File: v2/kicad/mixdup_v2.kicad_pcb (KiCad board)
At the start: 2 copper layers, 96.5 x 189.2 mm, 38 parts, among them IC1 Teensy3.2, IC2 74HC4051, IC3 74HC4051, IC4 74HC4051, IC5 74HC4051, J1 Conn_02x10_Counter_Clockwise, SW1 SW_SPST, SW10 SW_SPST, SW11 SW_SPST, SW12 SW_SPST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

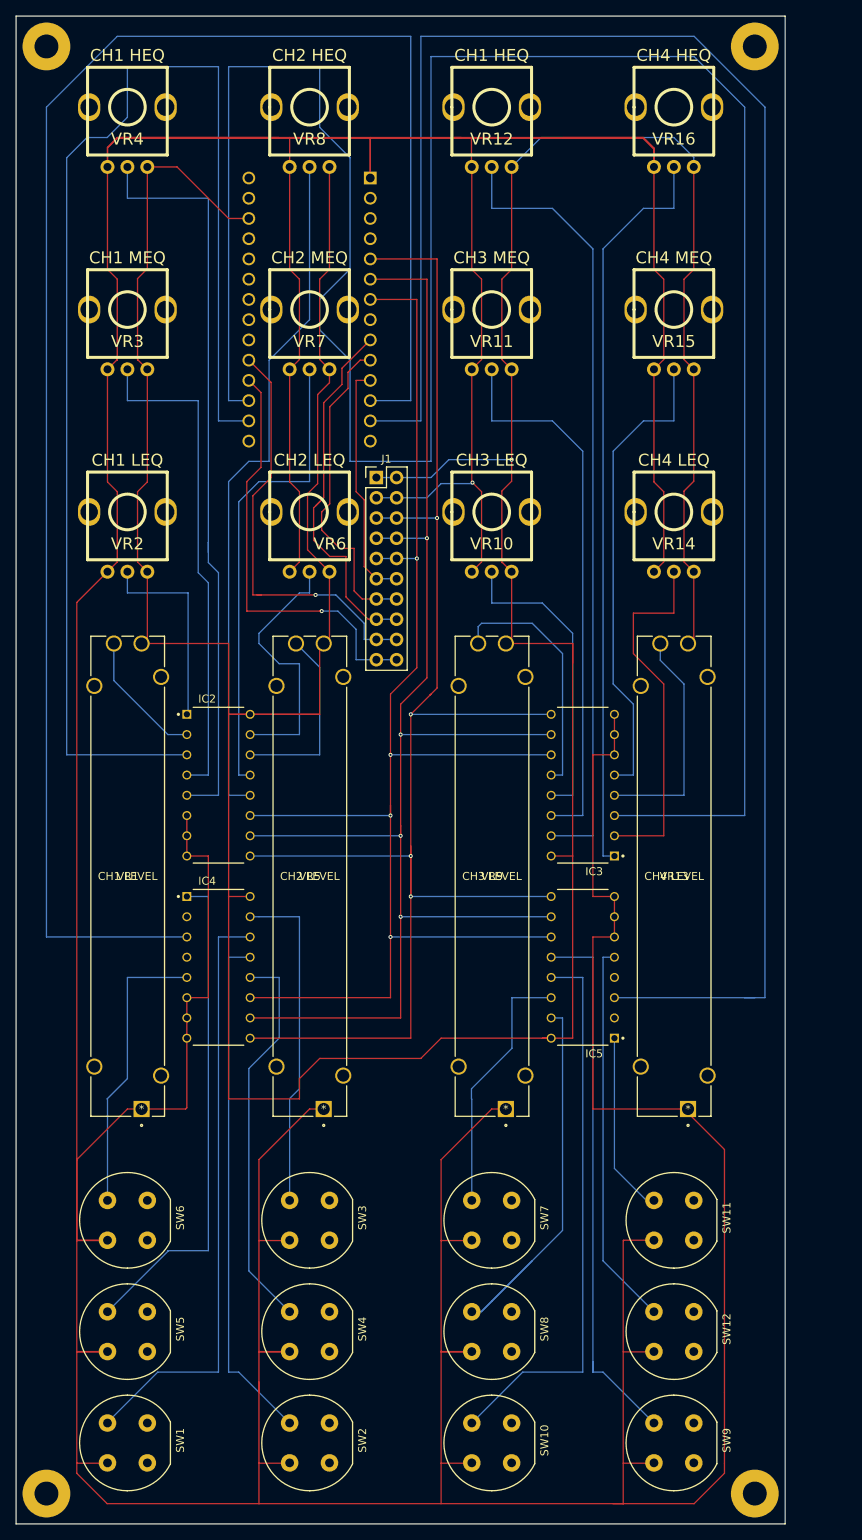
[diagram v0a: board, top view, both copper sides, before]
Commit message: components spaced out
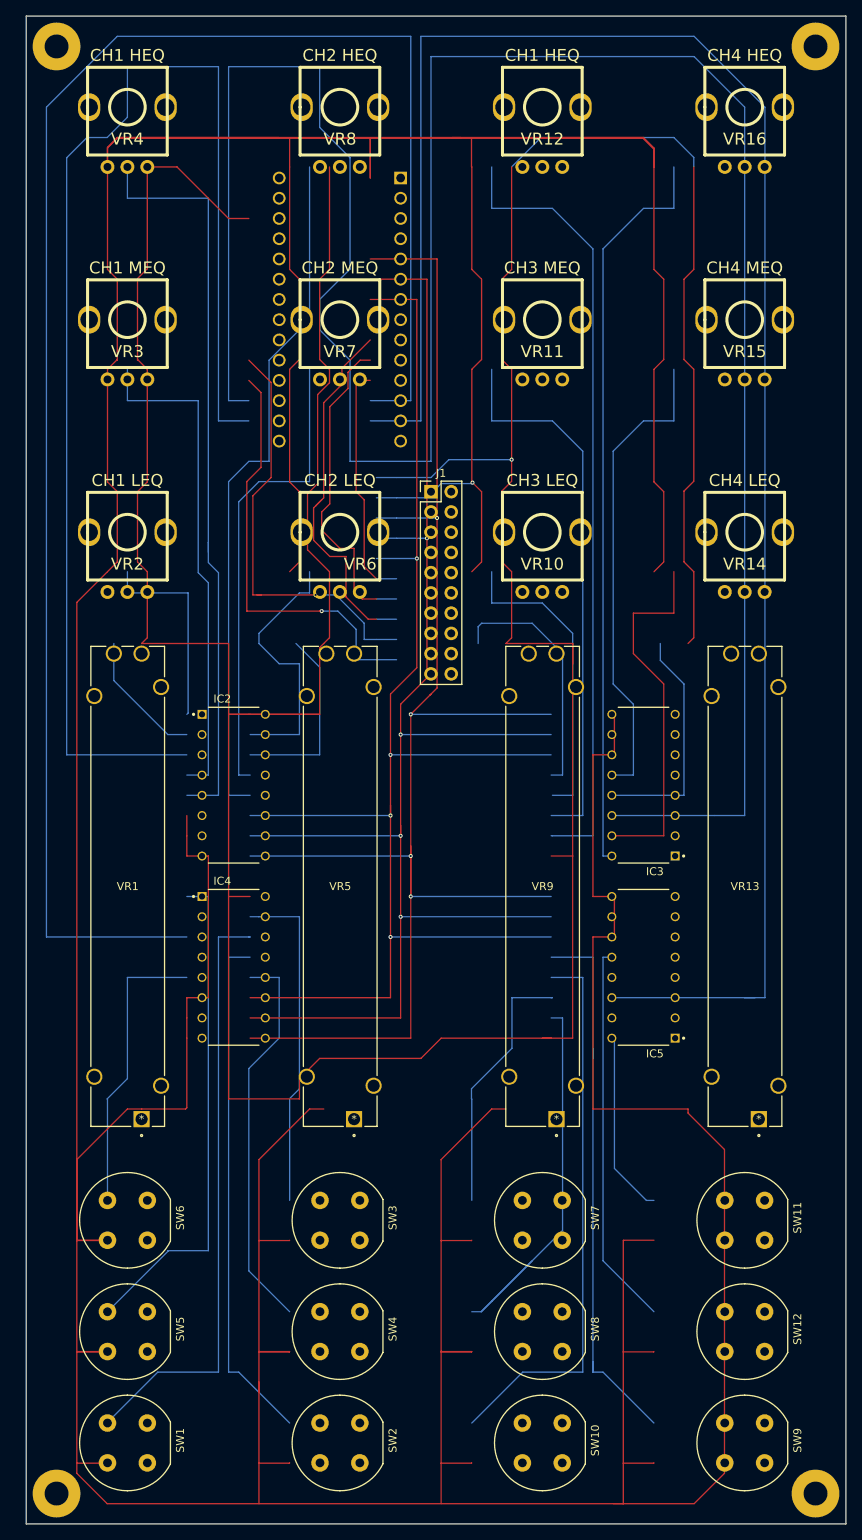
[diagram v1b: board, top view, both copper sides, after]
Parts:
- removed the ? at (222.2, 1139.2)
- removed the ? at (133.3, 1139.2)
- added ?: , MountingHole:MountingHole_3mm_Pad, F.Cu at (229.9, 1139.2)
- added ?: , MountingHole:MountingHole_3mm_Pad, F.Cu at (134.6, 1139.2)
- VR1: value CH1 LEVEL -> (none)
- VR13: value CH4 LEVEL -> (none)
- VR5: value CH2 LEVEL -> (none)
- VR9: value CH3 LEVEL -> (none)
- moved VR14 9.25 mm to (221.0, 1018.5)
- moved VR13 8.98 mm to (222.8, 1092.2)
- moved VR15 8.98 mm to (221.0, 991.9)
- moved SW11 8.89 mm to (221.0, 1104.9)
- moved SW12 8.89 mm to (221.0, 1118.9)
- moved SW9 8.89 mm to (221.0, 1132.8)
- moved VR16 8.89 mm to (221.0, 965.2)
- moved ? 7.62 mm to (229.9, 957.6)
- moved IC3 7.62 mm to (208.3, 1050.3)
- moved IC5 7.62 mm to (208.3, 1073.2)
- moved J1 7.08 mm to (181.6, 1013.5)
- moved VR10 6.84 mm to (195.6, 1018.5)
- moved VR11 6.48 mm to (195.6, 991.9)
- moved VR9 6.48 mm to (197.4, 1092.2)
- moved SW10 6.35 mm to (195.6, 1132.8)
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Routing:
- net VCC: track 524.7 -> 792.6 mm, vias 1 -> 2
- net (no net): track 0.00 -> 140.0 mm
- net Net-(IC3-Pad1): track 93.8 -> 0.00 mm
- net Net-(IC2-Pad12): track 87.3 -> 0.00 mm
- net Net-(IC3-Pad5): track 59.7 -> 0.00 mm
- net Net-(IC1-Pad23): track 54.1 -> 0.00 mm, vias 1 -> 0
- net Net-(IC5-Pad15): track 52.8 -> 0.00 mm
- net Net-(IC5-Pad12): track 70.2 -> 118.7 mm
- net Net-(IC5-Pad5): track 48.6 -> 0.00 mm
- net Net-(IC3-Pad15): track 98.9 -> 144.9 mm
- net Net-(IC3-Pad2): track 46.0 -> 0.00 mm
- net Net-(IC1-Pad9): track 46.7 -> 2.54 mm
- net Net-(IC2-Pad13): track 59.8 -> 103.9 mm
- net Net-(IC1-Pad10): track 40.7 -> 2.54 mm
- net Net-(IC3-Pad12): track 31.1 -> 59.7 mm
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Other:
- board size 96.5 x 189.2 mm -> 102.9 x 189.2 mm

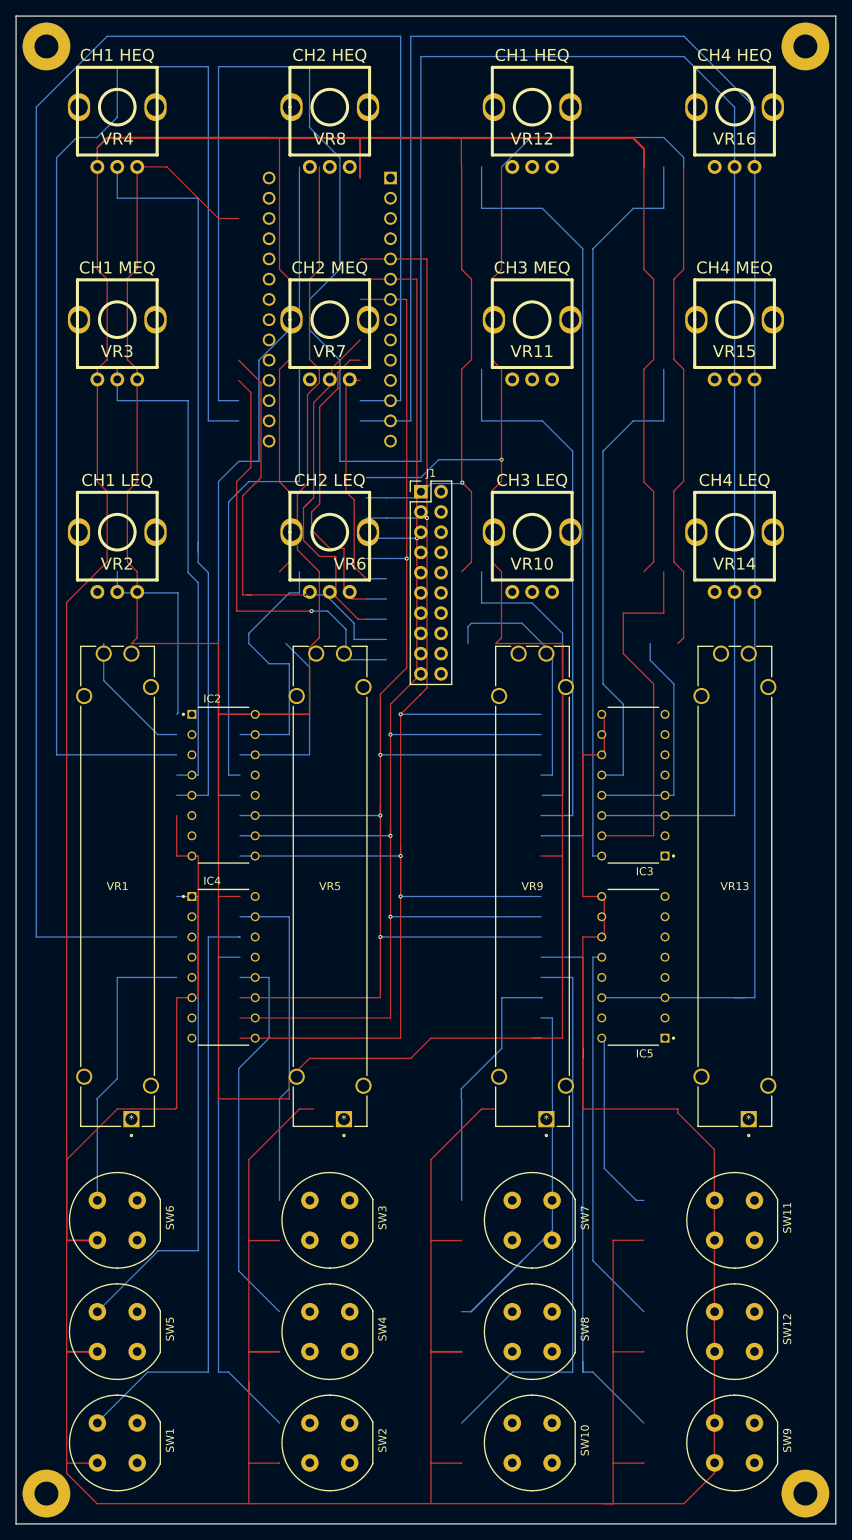
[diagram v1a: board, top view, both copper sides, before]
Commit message: better spacing, ICs on back
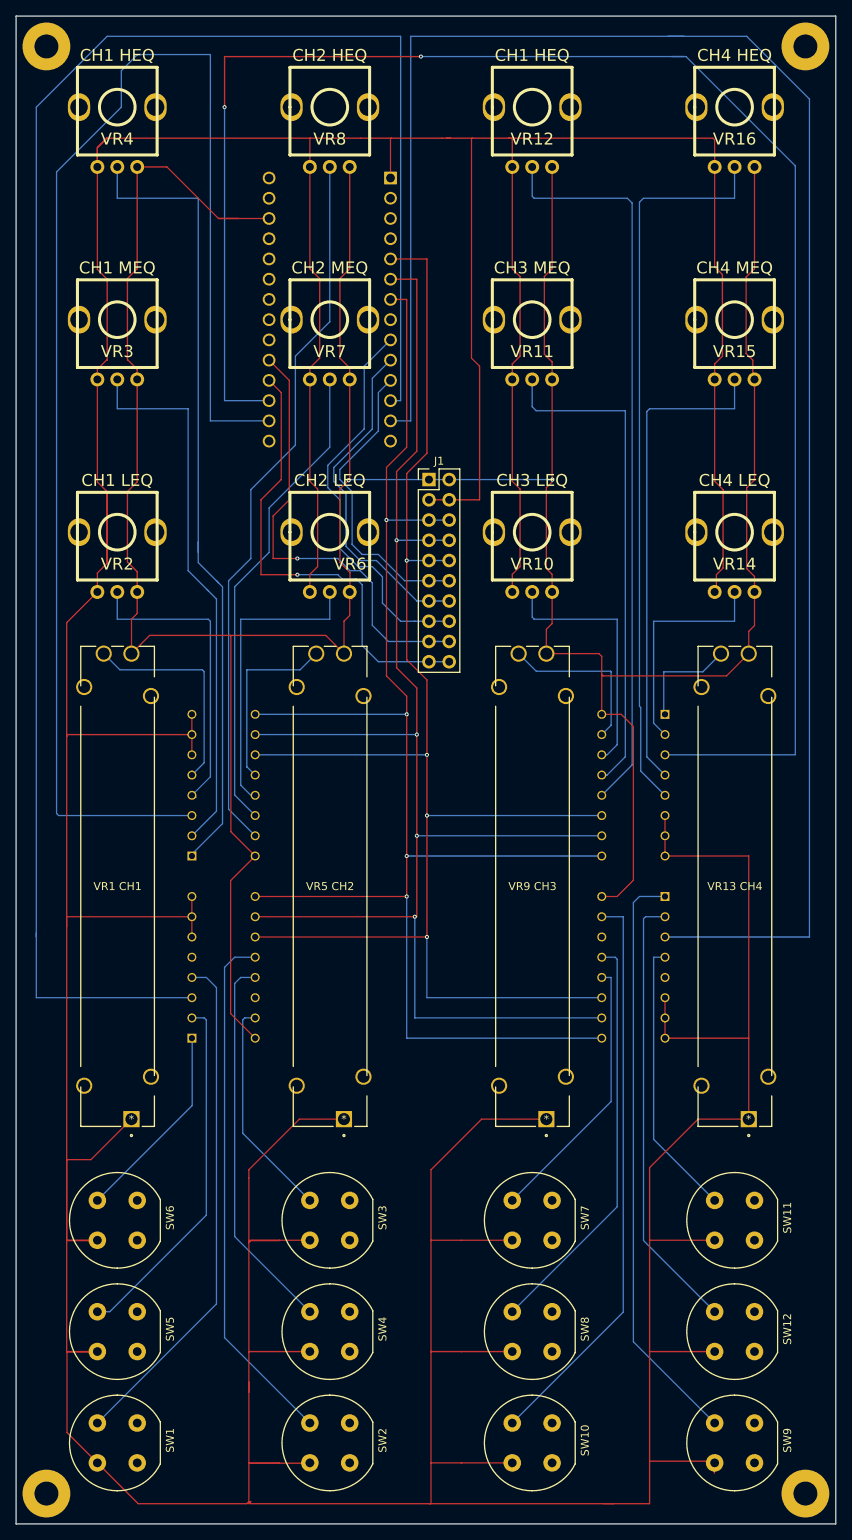
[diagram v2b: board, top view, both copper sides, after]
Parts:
- IC2, IC3, IC4, IC5: moved to B.Cu
- VR1 CH1: renamed from VR1
- VR13 CH4: renamed from VR13
- VR5 CH2: renamed from VR5
- VR9 CH3: renamed from VR9
- moved J1 1.83 mm to (182.6, 1011.9)
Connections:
- IC2 pad 11: Net-(IC1-Pad7) -> Net-(IC1-Pad5)
- IC2 pad 9: Net-(IC1-Pad5) -> Net-(IC1-Pad7)
- IC3 pad 11: Net-(IC1-Pad7) -> Net-(IC1-Pad5)
- IC3 pad 9: Net-(IC1-Pad5) -> Net-(IC1-Pad7)
- IC4 pad 11: Net-(IC1-Pad7) -> Net-(IC1-Pad5)
- IC4 pad 9: Net-(IC1-Pad5) -> Net-(IC1-Pad7)
- IC5 pad 11: Net-(IC1-Pad7) -> Net-(IC1-Pad5)
- IC5 pad 9: Net-(IC1-Pad5) -> Net-(IC1-Pad7)
- J1 pad 10: Net-(IC1-Pad7) -> Net-(IC1-Pad5)
- J1 pad 5: Net-(IC1-Pad5) -> Net-(IC1-Pad7)
- J1 pad 6: Net-(IC1-Pad5) -> Net-(IC1-Pad7)
- J1 pad 9: Net-(IC1-Pad7) -> Net-(IC1-Pad5)
- SW1 pad 1: Net-(IC4-Pad14) -> Net-(IC4-Pad4)
- SW10 pad 1: Net-(IC5-Pad13) -> Net-(IC5-Pad15)
- SW11 pad 1: Net-(IC5-Pad1) -> Net-(IC5-Pad4)
- SW12 pad 1: Net-(IC5-Pad5) -> Net-(IC5-Pad2)
- SW2 pad 1: Net-(IC4-Pad13) -> Net-(IC4-Pad12)
- SW4 pad 1: Net-(IC4-Pad12) -> Net-(IC4-Pad13)
- SW5 pad 1: Net-(IC4-Pad1) -> Net-(IC4-Pad2)
- SW6 pad 1: Net-(IC4-Pad5) -> Net-(IC4-Pad1)
- SW7 pad 1: Net-(IC5-Pad14) -> Net-(IC5-Pad12)
- SW8 pad 1: Net-(IC5-Pad15) -> Net-(IC5-Pad13)
- SW9 pad 1: Net-(IC5-Pad12) -> Net-(IC5-Pad1)
- VR1 CH1 pad 2: Net-(IC2-Pad2) -> Net-(IC2-Pad5)
- VR10 pad 2: Net-(IC3-Pad13) -> Net-(IC3-Pad14)
- VR11 pad 2: Net-(IC3-Pad14) -> Net-(IC3-Pad13)
- VR12 pad 2: Net-(IC3-Pad15) -> Net-(IC3-Pad12)
- VR13 CH4 pad 2: Net-(IC3-Pad4) -> Net-(IC3-Pad1)
- VR15 pad 2: Net-(IC3-Pad5) -> Net-(IC3-Pad4)
- VR16 pad 2: Net-(IC3-Pad1) -> Net-(IC3-Pad5)
- VR2 pad 2: Net-(IC2-Pad1) -> Net-(IC2-Pad4)
- VR3 pad 2: Net-(IC2-Pad4) -> Net-(IC2-Pad2)
- VR4 pad 2: Net-(IC2-Pad5) -> Net-(IC2-Pad1)
- VR5 CH2 pad 2: Net-(IC2-Pad14) -> Net-(IC2-Pad12)
- VR6 pad 2: Net-(IC2-Pad15) -> Net-(IC2-Pad13)
- VR7 pad 2: Net-(IC2-Pad13) -> Net-(IC2-Pad14)
- VR8 pad 2: Net-(IC2-Pad12) -> Net-(IC2-Pad15)
- VR9 CH3 pad 2: Net-(IC3-Pad12) -> Net-(IC3-Pad15)
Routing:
- net VCC: track 792.6 -> 447.3 mm
- net (no net): track 140.0 -> 0.00 mm
- net Net-(IC3-Pad15): track 144.9 -> 20.9 mm
- net Net-(IC1-Pad22): track 318.5 -> 217.9 mm, vias 0 -> 2
- net Net-(IC3-Pad5): track 0.00 -> 91.8 mm
- net Net-(IC5-Pad12): track 118.7 -> 34.3 mm
- net Net-(IC2-Pad1): track 25.6 -> 101.1 mm
- net Net-(IC4-Pad14): track 75.4 -> 0.00 mm
- net Net-(IC5-Pad1): track 0.00 -> 73.8 mm
- net Net-(IC5-Pad15): track 0.00 -> 72.0 mm
- net Net-(IC2-Pad5): track 94.8 -> 27.3 mm
- net Net-(IC2-Pad13): track 103.9 -> 37.8 mm
- net Net-(IC4-Pad4): track 0.00 -> 64.5 mm
- net Net-(IC1-Pad23): track 0.00 -> 58.7 mm, vias 0 -> 1
- net Net-(IC2-Pad15): track 33.6 -> 90.6 mm
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
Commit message: prototype ics on back better distro
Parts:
- removed the ? at (229.9, 1139.2)
- removed the ? at (134.6, 1139.2)
- added ?: , MountingHole:MountingHole_3mm_Pad, F.Cu at (134.4, 206.8)
- added ?: , MountingHole:MountingHole_3mm_Pad, F.Cu at (134.4, 37.6)
- J1: value Conn_02x10_Counter_Clockwise -> (none)
- SW1, SW10, SW11, SW12, SW2, SW3, SW4, SW5, SW6, SW7, SW8, SW9: value SW_SPST -> (none)
- VR12, VR4: value CH1 HEQ -> (none)
- VR16: value CH4 HEQ -> (none)
- VR8: value CH2 HEQ -> (none)
- moved SW3 932.2 mm to (94.5, 175.8)
- moved SW6 932.2 mm to (67.8, 175.8)
- moved SW1 932.2 mm to (67.8, 203.7)
- moved SW2 932.2 mm to (94.5, 203.7)
- moved SW4 932.2 mm to (94.5, 189.7)
- moved SW5 932.2 mm to (67.8, 189.7)
- moved SW7 932.1 mm to (121.2, 175.8)
- moved SW10 932.1 mm to (121.2, 203.7)
- moved SW8 932.1 mm to (121.2, 189.7)
- moved SW11 932.0 mm to (147.8, 175.8)
- moved SW9 932.0 mm to (147.8, 203.7)
- moved SW12 932.0 mm to (147.8, 189.7)
- moved VR1 CH1 930.4 mm to (69.6, 164.8)
- moved VR5 CH2 930.4 mm to (96.3, 164.8)
- moved VR9 CH3 930.3 mm to (122.9, 164.8)
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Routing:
- net Earth: track 973.5 -> 823.9 mm, vias 0 -> 1
- net VCC: track 447.3 -> 490.7 mm, vias 2 -> 1
- net Net-(IC1-Pad12): track 228.2 -> 203.1 mm
- net Net-(IC1-Pad13): track 229.4 -> 205.4 mm
- net Net-(IC1-Pad21): track 179.0 -> 159.9 mm
- net Net-(IC1-Pad22): track 217.9 -> 206.6 mm
- net Net-(IC1-Pad10): track 42.7 -> 47.4 mm
- net Net-(IC4-Pad2): track 45.1 -> 40.6 mm
- net Net-(IC1-Pad6): track 192.0 -> 196.2 mm
- net Net-(IC1-Pad5): track 191.9 -> 196.1 mm
- net Net-(IC1-Pad9): track 50.3 -> 54.3 mm
- net Net-(IC1-Pad7): track 191.7 -> 195.7 mm
- net Net-(IC4-Pad15): track 27.8 -> 23.9 mm
- net Net-(IC4-Pad13): track 48.0 -> 44.3 mm
- net Net-(IC1-Pad23): track 58.7 -> 62.4 mm
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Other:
- board size 102.9 x 189.2 mm -> 101.6 x 177.8 mm
